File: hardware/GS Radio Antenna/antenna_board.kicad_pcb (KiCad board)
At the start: 2 copper layers, 88.9 x 92.5 mm, 27 parts, among them J1 Conn_01x02_Socket, U10 IRF4905PBF, U11 IRF4905PBF, U12 IRF4905PBF, U2 ESP32-DEVKITC, U3 LM3940IT-3.3/NOPB, U4 TLC5916IN, U5 TLC5916IN, U6 TLC5916IN, U9 IRF4905PBF

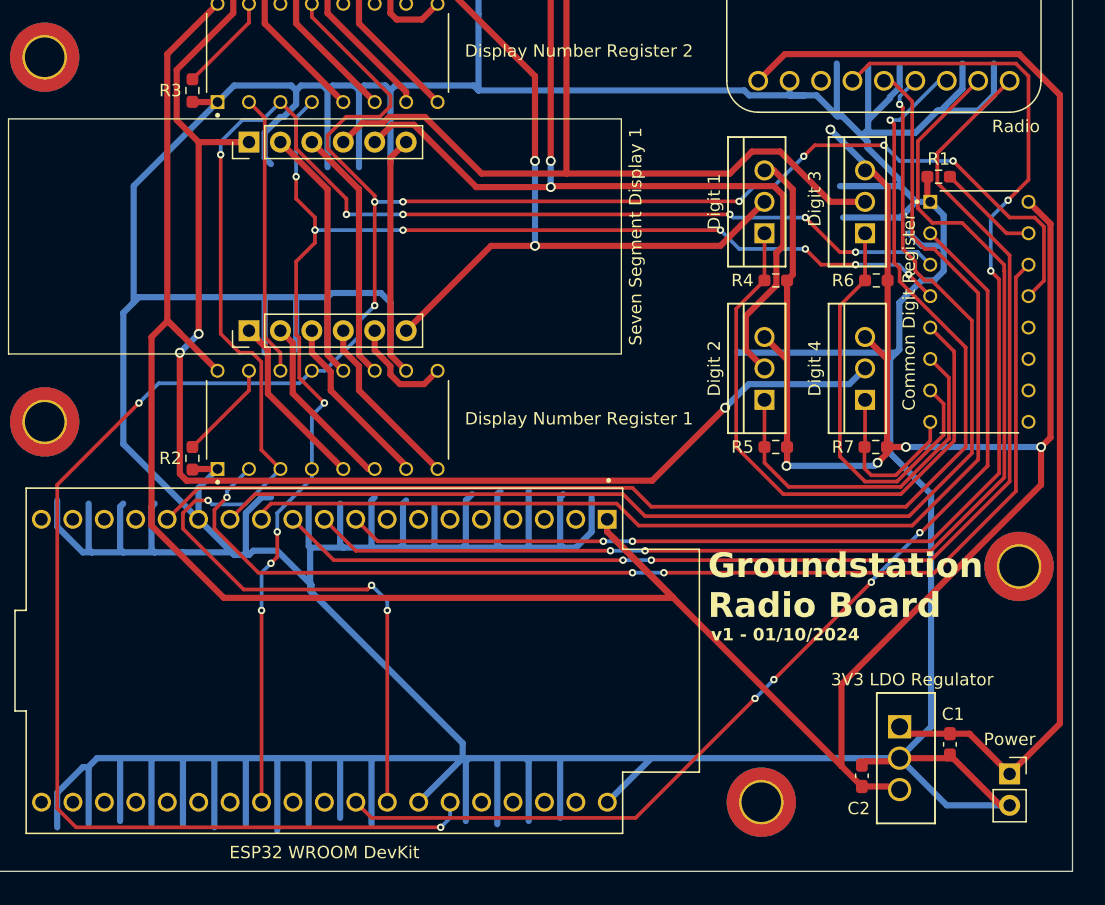
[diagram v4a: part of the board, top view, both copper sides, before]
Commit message: Add logo and switch displays to HSPI radio
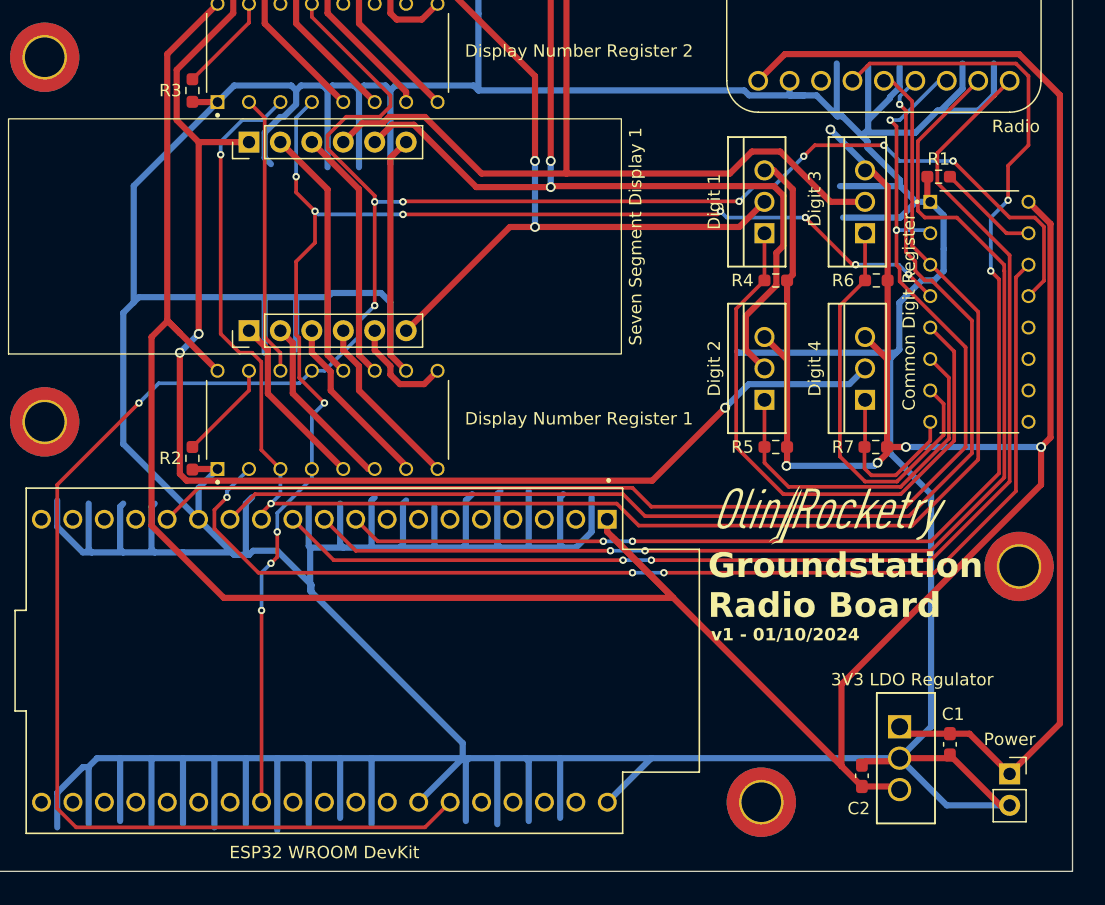
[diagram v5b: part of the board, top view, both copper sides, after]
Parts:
- added G***: LOGO, LOGO, F.Cu at (169.7, 105.4)
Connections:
- U2 pad 30: /SDI -> unconnected-(U2-IO18-Pad30)
- U2 pad 31: /CLK -> unconnected-(U2-IO19-Pad31)
- U4 pad 2: /SDI -> /MOSI
- U4 pad 3: /CLK -> /SCK
- U5 pad 3: /CLK -> /SCK
- U6 pad 3: /CLK -> /SCK
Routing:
- net /CLK: track 141.7 -> 0.00 mm, vias 9 -> 0
- net /SDI: track 84.1 -> 0.00 mm, vias 4 -> 0
- net /SCK: track 96.3 -> 134.2 mm, vias 0 -> 2
- net GND: track 730.8 -> 726.4 mm
- net /MOSI: track 103.0 -> 105.9 mm, vias 1 -> 2
- net /CTL1: track 61.2 -> 59.7 mm
- net /LE: track 113.3 -> 114.2 mm
- net /OE: track 189.6 -> 188.9 mm, vias 9 -> 8

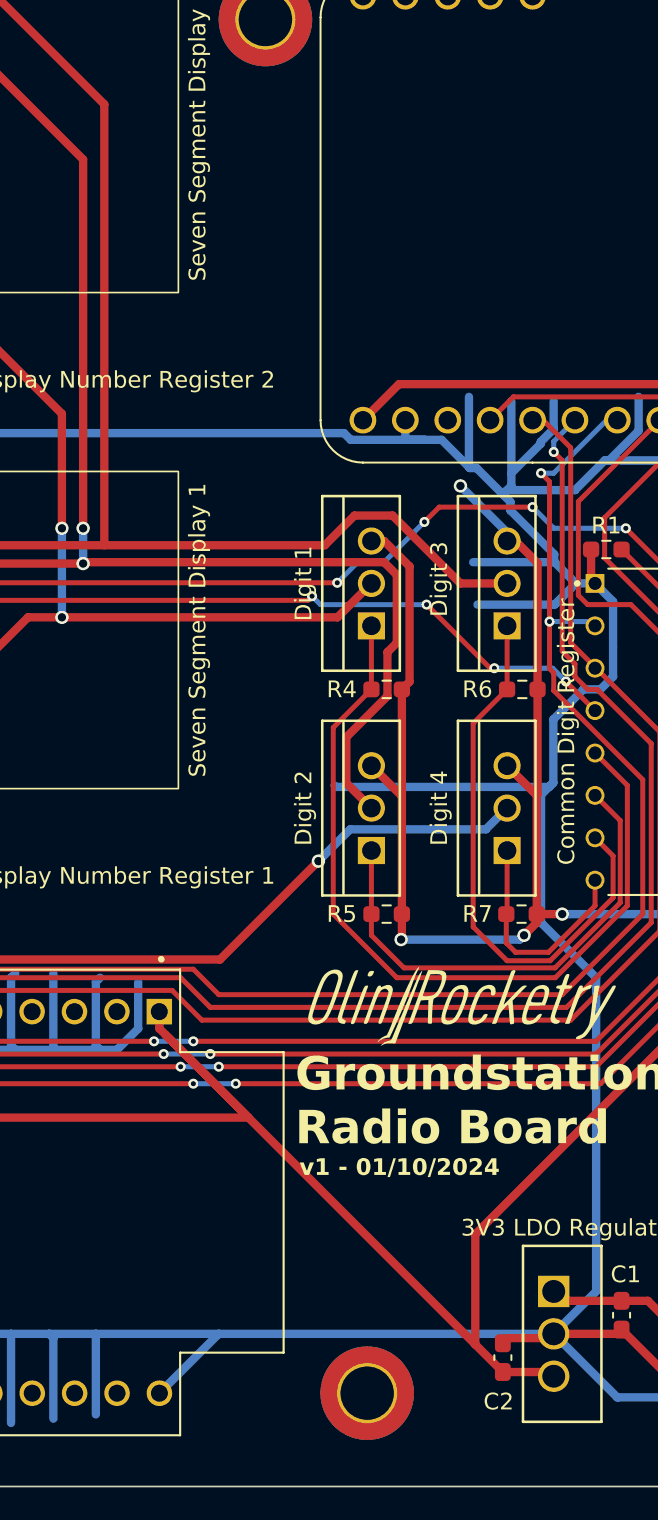
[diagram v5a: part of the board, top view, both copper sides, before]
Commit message: Changed capacitor
Changed the large capacitor for the voltage regulator to reflect BOM
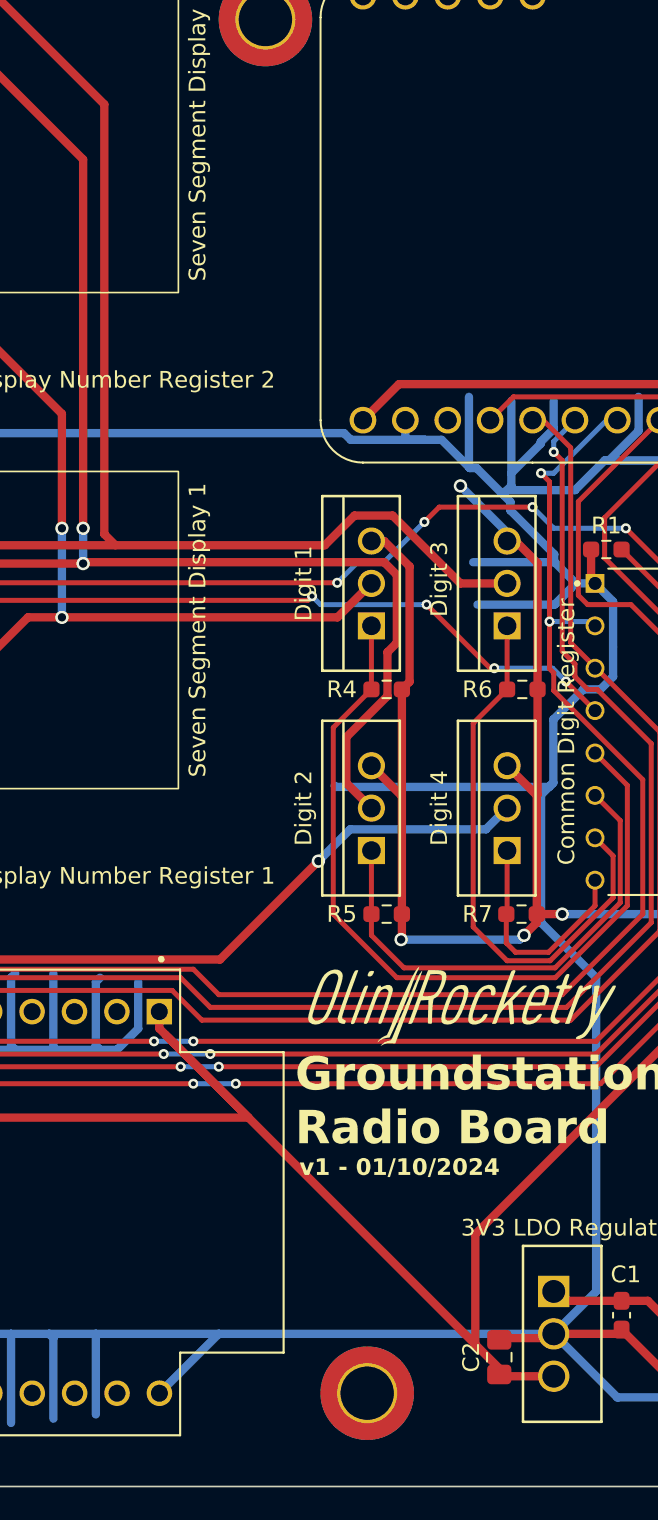
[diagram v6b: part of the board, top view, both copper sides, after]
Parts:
- C2: footprint Capacitor_SMD:C_0603_1608Metric_Pad1.08x0.95mm_HandSolder -> Capacitor_SMD:C_0805_2012Metric_Pad1.18x1.45mm_HandSolder
- moved C2 0.22 mm to (172.0, 126.6)
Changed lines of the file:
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@@
     )
   )
-  (footprint "Capacitor_SMD:C_0603_1608Metric_Pad1.08x0.95mm_HandSolder" (layer "F.Cu")
-    (at 172.212 126.6455 90)
-    (descr "Capacitor SMD 0603 (1608 Metric), square (rectangular) end terminal, IPC_7351 nominal with elongated pad for handsoldering. (Body size source: IPC-SM-782 page 76, https://www.pcb-3d.com/wordpress/wp-content/uploads/ipc-sm-782a_amendment_1_and_2.pdf), generated with kicad-footprint-generator")
+  (footprint "Capacitor_SMD:C_0805_2012Metric_Pad1.18x1.45mm_HandSolder" (layer "F.Cu")
+    (at 171.996481 126.618501 90)
+    (descr "Capacitor SMD 0805 (2012 Metric), square (rectangular) end terminal, IPC_7351 nominal with elongated pad for handsoldering. (Body size source: IPC-SM-782 page 76, https://www.pcb-3d.com/wordpress/wp-content/uploads/ipc-sm-782a_amendment_1_and_2.pdf, https://docs.google.com/spreadsheets/d/1BsfQQcO9C6DZCsRaXUlFlo91Tg2WpOkGARC1WS5S8t0/edit?usp=sharing), generated with kicad-footprint-generator")
     (tags "capacitor handsolder")
     (property "Sheetfile" "antenna_board.kicad_sch")
@@
     (property "ki_keywords" "cap capacitor")
     (attr smd)
-    (fp_text reference "C2" (at -2.6405 -0.254 180) (layer "F.SilkS")
+    (fp_text reference "C2" (at 0 -1.68 90) (layer "F.SilkS")
         (effects (font (size 1 1) (thickness 0.15)))
     )
-    (fp_text value "33 uF" (at 0 1.43 90) (layer "F.Fab")
+    (fp_text value "33 uF" (at 0 1.68 90) (layer "F.Fab")
         (effects (font (size 1 1) (thickness 0.15)))
     )
     (fp_text user "${REFERENCE}" (at 0 0 90) (layer "F.Fab")
-        (effects (font (size 0.4 0.4) (thickness 0.06)))
+        (effects (font (size 0.5 0.5) (thickness 0.08)))
     )
-    (fp_line (start -0.146267 -0.51) (end 0.146267 -0.51)
+    (fp_line (start -0.261252 -0.735) (end 0.261252 -0.735)
       (stroke (width 0.12) (type solid)) (layer "F.SilkS"))
-    (fp_line (start -0.146267 0.51) (end 0.146267 0.51)
+    (fp_line (start -0.261252 0.735) (end 0.261252 0.735)
       (stroke (width 0.12) (type solid)) (layer "F.SilkS"))
-    (fp_line (start -1.65 -0.73) (end 1.65 -0.73)
+    (fp_line (start -1.88 -0.98) (end 1.88 -0.98)
       (stroke (width 0.05) (type solid)) (layer "F.CrtYd"))
-    (fp_line (start -1.65 0.73) (end -1.65 -0.73)
+    (fp_line (start -1.88 0.98) (end -1.88 -0.98)
       (stroke (width 0.05) (type solid)) (layer "F.CrtYd"))
-    (fp_line (start 1.65 -0.73) (end 1.65 0.73)
+    (fp_line (start 1.88 -0.98) (end 1.88 0.98)
       (stroke (width 0.05) (type solid)) (layer "F.CrtYd"))
-    (fp_line (start 1.65 0.73) (end -1.65 0.73)
+    (fp_line (start 1.88 0.98) (end -1.88 0.98)
       (stroke (width 0.05) (type solid)) (layer "F.CrtYd"))
-    (fp_line (start -0.8 -0.4) (end 0.8 -0.4)
+    (fp_line (start -1 -0.625) (end 1 -0.625)
       (stroke (width 0.1) (type solid)) (layer "F.Fab"))
-    (fp_line (start -0.8 0.4) (end -0.8 -0.4)
+    (fp_line (start -1 0.625) (end -1 -0.625)
       (stroke (width 0.1) (type solid)) (layer "F.Fab"))
-    (fp_line (start 0.8 -0.4) (end 0.8 0.4)
+    (fp_line (start 1 -0.625) (end 1 0.625)
       (stroke (width 0.1) (type solid)) (layer "F.Fab"))
-    (fp_line (start 0.8 0.4) (end -0.8 0.4)
+    (fp_line (start 1 0.625) (end -1 0.625)
       (stroke (width 0.1) (type solid)) (layer "F.Fab"))
-    (pad "1" smd roundrect (at -0.8625 0 90) (size 1.075 0.95) (layers "F.Cu" "F.Paste" "F.Mask") (roundrect_rratio 0.25)
+    (pad "1" smd roundrect (at -1.0375 0 90) (size 1.175 1.45) (layers "F.Cu" "F.Paste" "F.Mask") (roundrect_rratio 0.212766)
       (net 6 "/3.3V") (pintype "passive"))
-    (pad "2" smd roundrect (at 0.8625 0 90) (size 1.075 0.95) (layers "F.Cu" "F.Paste" "F.Mask") (roundrect_rratio 0.25)
+    (pad "2" smd roundrect (at 1.0375 0 90) (size 1.175 1.45) (layers "F.Cu" "F.Paste" "F.Mask") (roundrect_rratio 0.212766)
       (net 2 "GND") (pintype "passive"))
-    (model "${KICAD6_3DMODEL_DIR}/Capacitor_SMD.3dshapes/C_0603_1608Metric.wrl"
+    (model "${KICAD6_3DMODEL_DIR}/Capacitor_SMD.3dshapes/C_0805_2012Metric.wrl"
       (offset (xyz 0 0 0))
       (scale (xyz 1 1 1))
@@
   (segment (start 171.196 94.996) (end 172.466 93.726) (width 0.5) (layer "B.Cu") (net 5))
   (segment (start 163.068 94.996) (end 171.196 94.996) (width 0.5) (layer "B.Cu") (net 5))
-  (segment (start 175.006 127.508) (end 175.26 127.762) (width 0.5) (layer "F.Cu") (net 6))
   (segment (start 166.163 93.011) (end 166.163 100.076) (width 0.5) (layer "F.Cu") (net 6))
   (segment (start 170.561 125.857) (end 152.019 107.315) (width 0.5) (layer "F.Cu") (net 6))
@@
   (segment (start 120.142 64.262) (end 116.078 68.326) (width 0.5) (layer "F.Cu") (net 6))
   (segment (start 164.338 77.724) (end 165.1 77.724) (width 0.5) (layer "F.Cu") (net 6))
-  (segment (start 172.212 127.508) (end 175.006 127.508) (width 0.5) (layer "F.Cu") (net 6))
   (segment (start 166.163 101.553) (end 166.116 101.6) (width 0.5) (layer "F.Cu") (net 6))
   (segment (start 114.808 91.186) (end 114.808 106.426) (width 0.5) (layer "F.Cu") (net 6))
@@
   (segment (start 173.482 101.346) (end 174.244 100.584) (width 0.5) (layer "F.Cu") (net 6))
   (segment (start 156.972 112.268) (end 152.146 107.442) (width 0.5) (layer "F.Cu") (net 6))
+  (segment (start 171.996481 127.292481) (end 170.561 125.857) (width 0.5) (layer "F.Cu") (net 6))
   (segment (start 187.452 82.042) (end 187.452 99.314) (width 0.5) (layer "F.Cu") (net 6))
   (segment (start 117.094 90.866) (end 116.111 89.883) (width 0.5) (layer "F.Cu") (net 6))
@@
   (segment (start 164.338 91.186) (end 166.163 93.011) (width 0.5) (layer "F.Cu") (net 6))
   (segment (start 174.291 79.041) (end 174.291 86.614) (width 0.5) (layer "F.Cu") (net 6))
-  (segment (start 172.212 127.508) (end 170.561 125.857) (width 0.5) (layer "F.Cu") (net 6))
   (segment (start 116.078 68.326) (end 116.078 89.85) (width 0.5) (layer "F.Cu") (net 6))
   (segment (start 152.019 107.315) (end 151.628 106.924) (width 0.5) (layer "F.Cu") (net 6))
+  (segment (start 175.26 127.762) (end 172.10248 127.762) (width 0.5) (layer "F.Cu") (net 6))
   (segment (start 174.291 86.614) (end 174.291 92.917) (width 0.5) (layer "F.Cu") (net 6))
   (segment (start 116.078 89.85) (end 117.094 90.866) (width 0.5) (layer "F.Cu") (net 6))
   (segment (start 114.808 106.426) (end 120.65 112.268) (width 0.5) (layer "F.Cu") (net 6))
+  (segment (start 172.10248 127.762) (end 171.996481 127.656001) (width 0.5) (layer "F.Cu") (net 6))
+  (segment (start 171.996481 127.656001) (end 171.996481 127.292481) (width 0.5) (layer "F.Cu") (net 6))
   (segment (start 186.69 103.124) (end 170.561 119.253) (width 0.5) (layer "F.Cu") (net 6))
   (segment (start 166.163 86.614) (end 166.163 93.011) (width 0.5) (layer "F.Cu") (net 6))
@@
   (segment (start 133.479288 73.914) (end 131.826 73.914) (width 0.5) (layer "F.Cu") (net 18))
   (segment (start 136.906 73.406) (end 133.987288 73.406) (width 0.5) (layer "F.Cu") (net 18))
-  (segment (start 148.336 51.562) (end 148.336 77.978) (width 0.5) (layer "F.Cu") (net 18))
   (segment (start 172.466 80.264) (end 169.672 80.264) (width 0.5) (layer "F.Cu") (net 18))
+  (segment (start 132.588 43.434) (end 140.208 43.434) (width 0.5) (layer "F.Cu") (net 18))
   (segment (start 133.987288 73.406) (end 133.479288 73.914) (width 0.5) (layer "F.Cu") (net 18))
   (segment (start 161.544 77.978) (end 141.478 77.978) (width 0.5) (layer "F.Cu") (net 18))
-  (segment (start 140.208 43.434) (end 148.336 51.562) (width 0.5) (layer "F.Cu") (net 18))
+  (segment (start 148.336 51.562) (end 148.336 77.314) (width 0.5) (layer "F.Cu") (net 18))
   (segment (start 163.322 76.2) (end 161.544 77.978) (width 0.5) (layer "F.Cu") (net 18))
   (segment (start 141.478 77.978) (end 136.906 73.406) (width 0.5) (layer "F.Cu") (net 18))
   (segment (start 131.826 73.914) (end 130.302 75.438) (width 0.5) (layer "F.Cu") (net 18))
-  (segment (start 130.302 45.72) (end 132.588 43.434) (width 0.5) (layer "F.Cu") (net 18))
+  (segment (start 148.336 77.314) (end 149 77.978) (width 0.5) (layer "F.Cu") (net 18))
   (segment (start 169.672 80.264) (end 165.608 76.2) (width 0.5) (layer "F.Cu") (net 18))
-  (segment (start 132.588 43.434) (end 140.208 43.434) (width 0.5) (layer "F.Cu") (net 18))
+  (segment (start 130.302 45.72) (end 132.588 43.434) (width 0.5) (layer "F.Cu") (net 18))
+  (segment (start 140.208 43.434) (end 148.336 51.562) (width 0.5) (layer "F.Cu") (net 18))
   (segment (start 165.608 76.2) (end 163.322 76.2) (width 0.5) (layer "F.Cu") (net 18))
   (segment (start 185.674 82.804) (end 183.896 82.804) (width 0.3) (layer "F.Cu") (net 19))
